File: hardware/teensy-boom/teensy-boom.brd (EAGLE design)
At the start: 160 x 100 mm, 5 parts

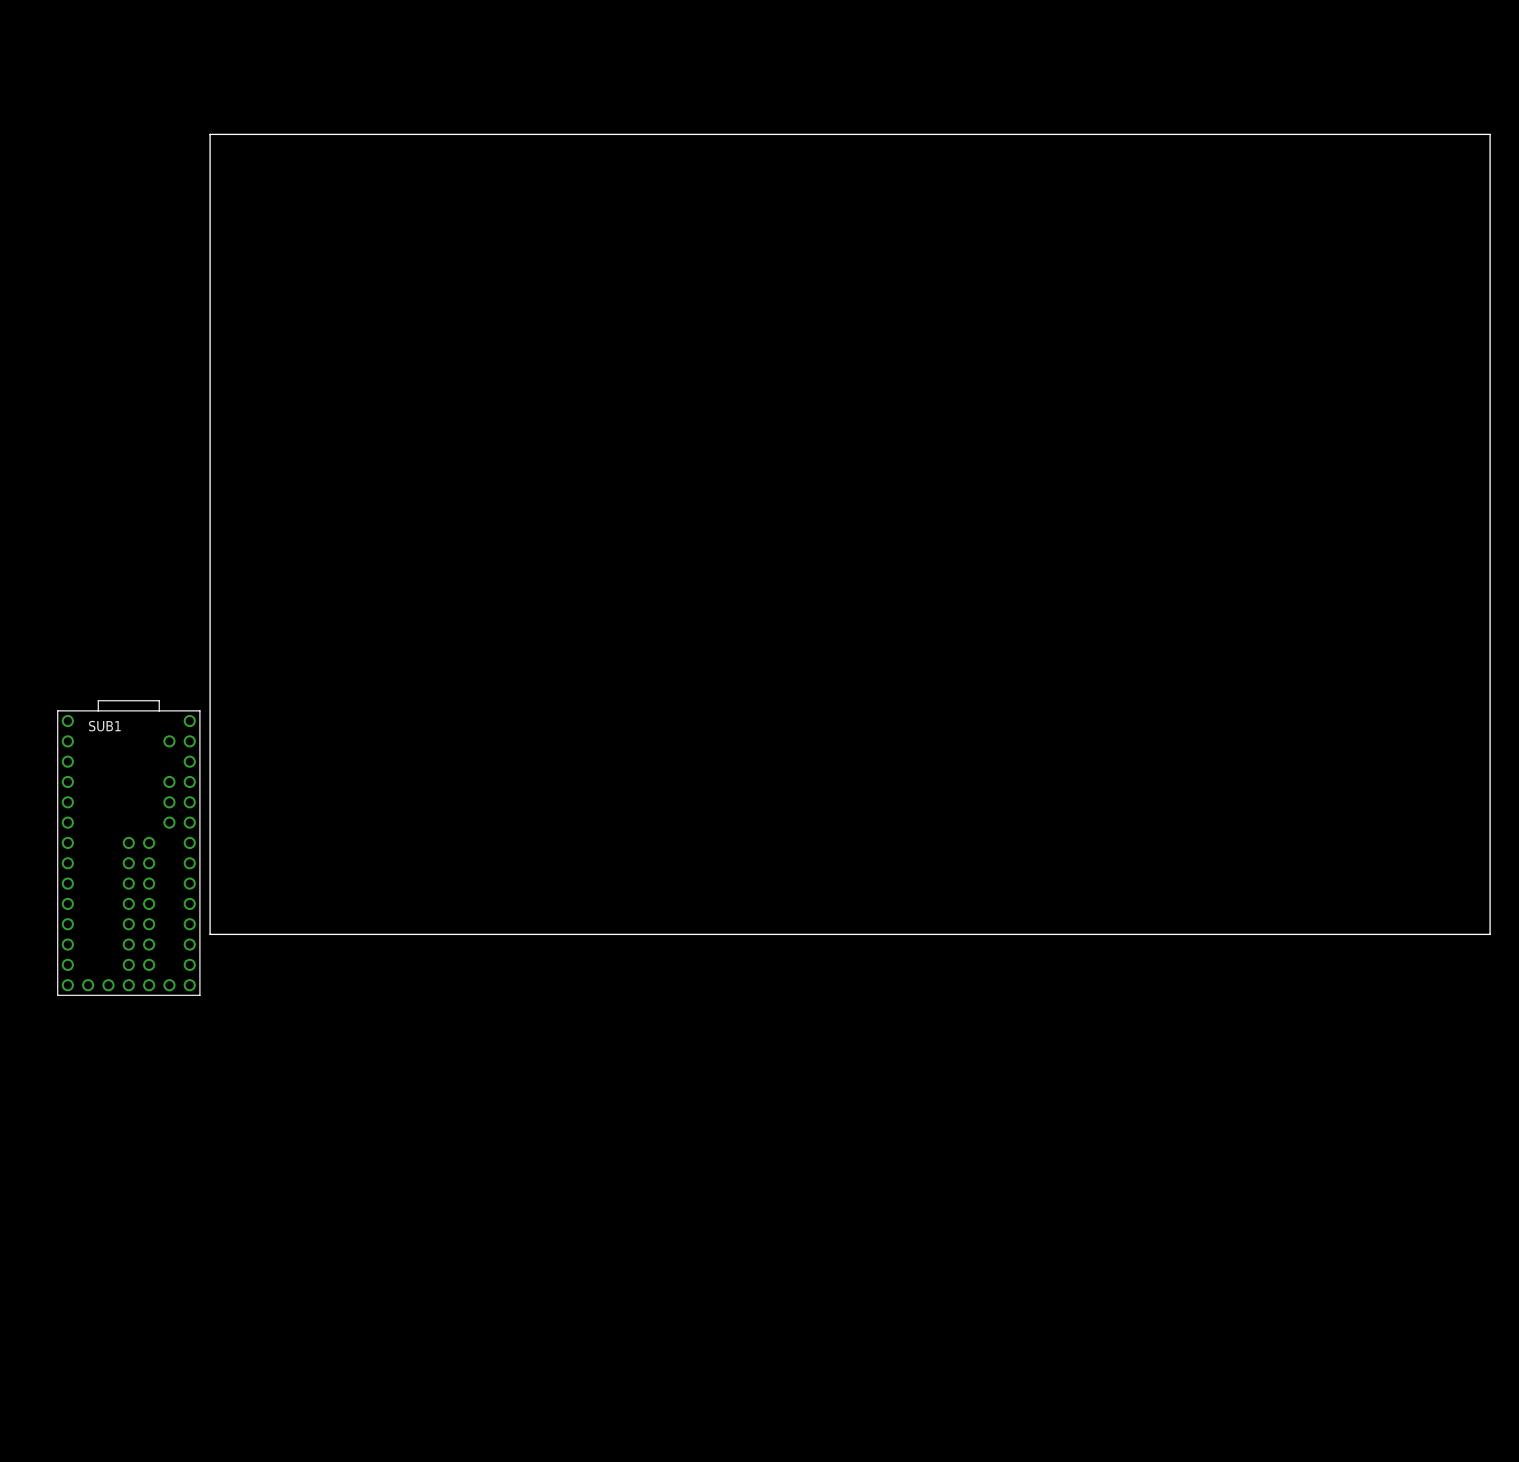
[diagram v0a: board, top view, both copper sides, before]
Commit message: More PCB work
Added knobs, buttons, connectors, MIDI.

Basic PCB alignment in place...~6"x4"
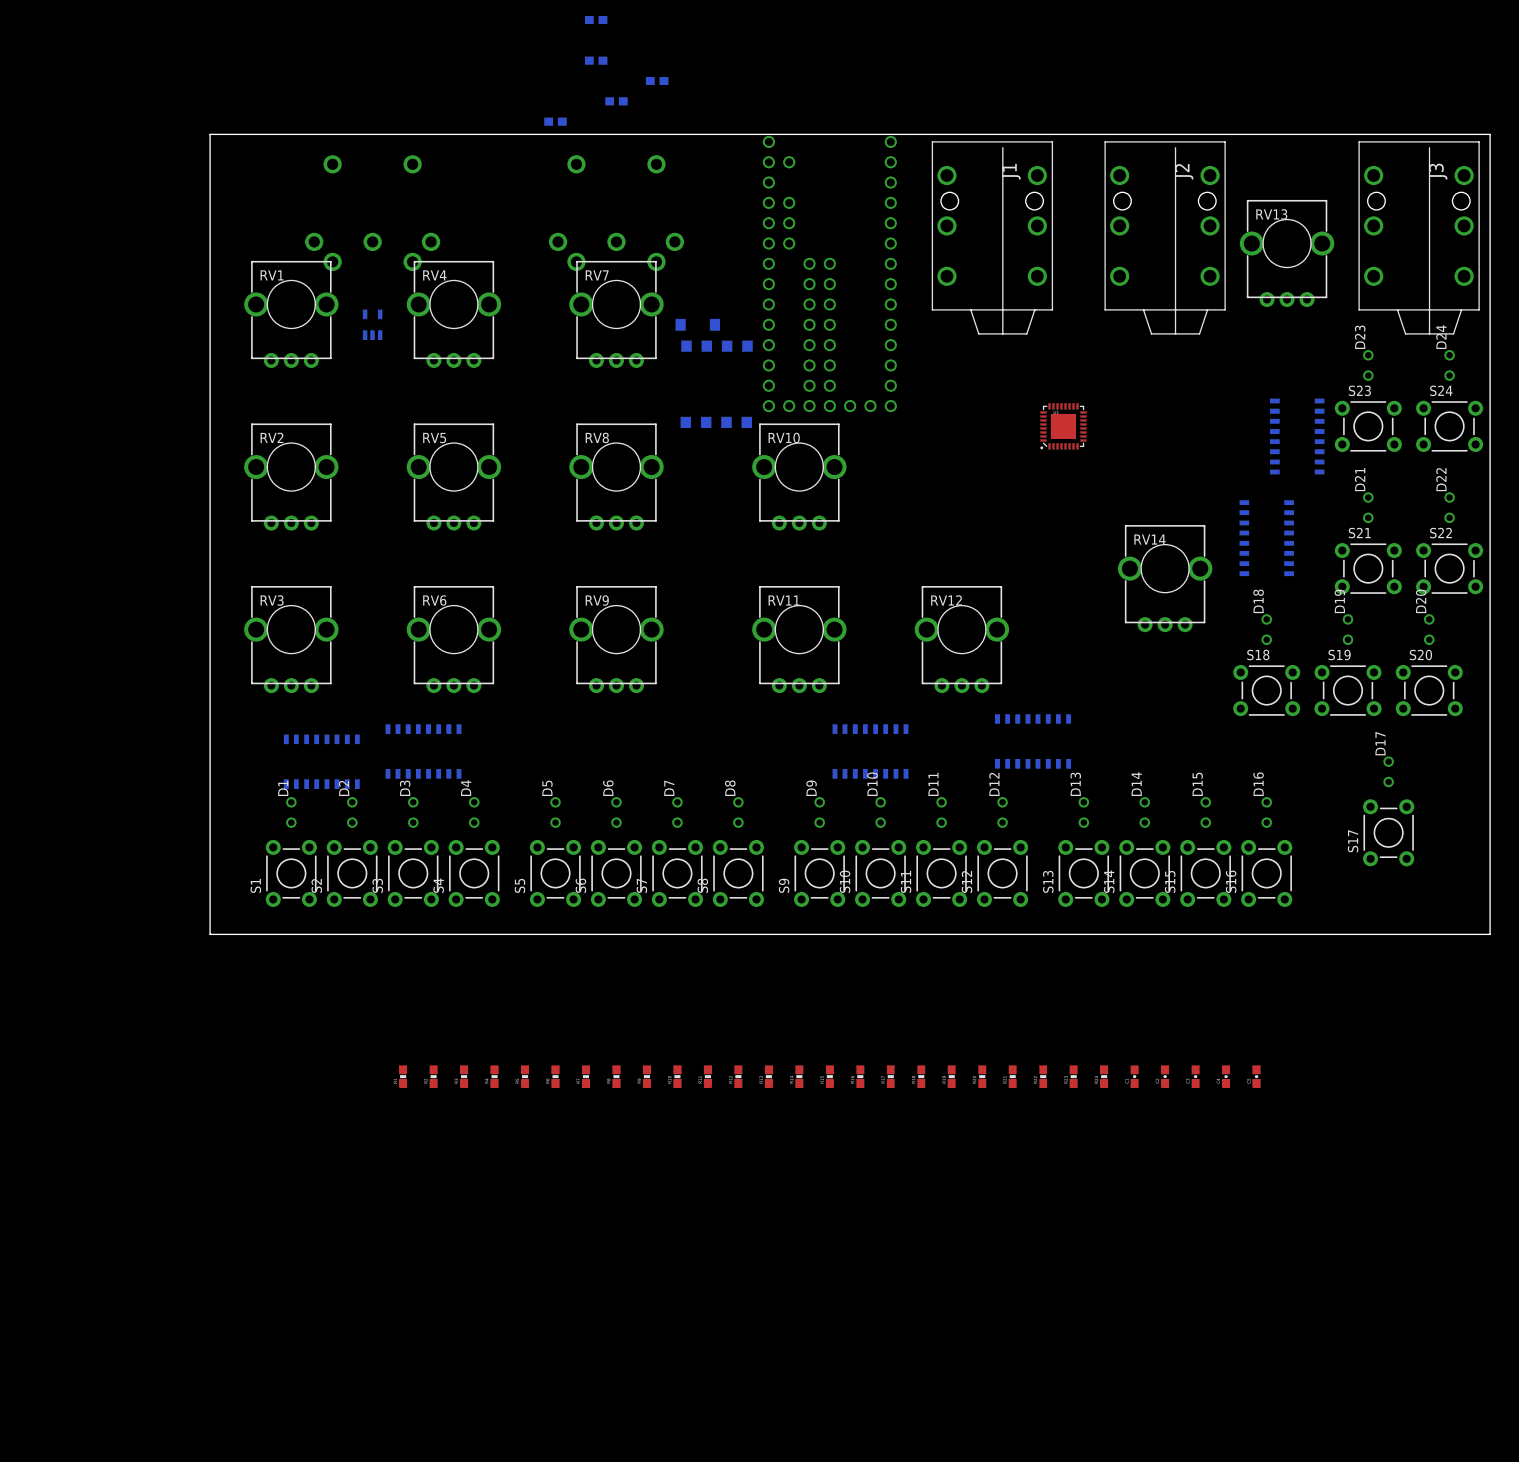
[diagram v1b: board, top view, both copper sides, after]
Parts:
- added C1, C2, C3, C4, C5, C6: 0.1uF, SparkFun-Capacitors:0603-CAP
- added D1, D10, D11, D12, D13, D14, D15, D16, D17, D18, D19, D2, D20, D21, D22, D23, D24, D3, D4, D5, D6, D7, D8, D9: (no value), SparkFun-LED:LED3MM-NS
- added D25: MBRA140, SparkFun-DiscreteSemi:SMA-DIODE
- added J1, J2, J3: AUDIO-JACK4-.25-HORIZ-TRS, SparkFun-Connectors:AUDIO-JACK-.25-INCH-HORIZ-PTH
- added J4, J5: 5-PIN-CIRCULAR-DINNEW, Testing:5-PIN-DIN-RA-PCB-NEW
- added R1, R10, R11, R12, R13, R14, R15, R16, R17, R18, R19, R2, R20, R21, R22, R23, R24, R3, R4, R5, R6, R7, R8, R9: 330, SparkFun-Resistors:0603-RES
- added R25, R26, R27, R28: 220, SparkFun-Resistors:0603-RES
- added RV1, RV10, RV11, RV12, RV13, RV14, RV2, RV3, RV4, RV5, RV6, RV7, RV8, RV9: (no value), SparkFun-Electromechanical:ALPS_POT_KIT
- added S1, S10, S11, S12, S13, S14, S15, S16, S17, S18, S19, S2, S20, S21, S22, S23, S24, S3, S4, S5, S6, S7, S8, S9: 6mm-TACT, SparkFun-Electromechanical:TACTILE-PTH
- added U1: SGTL5000, teensy-synth:QFN-32
- added U2, U3, U4: 74hc165, teensy-synth:SO16
- added U5, U6, U7: 74hc595, teensy-synth:SO16
- added U8: 6N138M, SparkFun-DiscreteSemi:8-SMD
- added U9: 74AHC1G125, SparkFun-DigitalIC:SOT23-5
- moved SUB1 127.9 mm to (86.4, 64.8), flipped to the bottom
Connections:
- new net 5V: R26.2, R28.2, U8.8, U9.5
- new net GND: J5.2, U8.5, U9.1, U9.3
- new net N$1: U9.2
- new net N$2: J4.4, R25.1
- new net N$3: D25.C, R25.2, U8.2
- new net N$4: D25.A, J4.5, U8.3
- new net N$5: R26.1, U8.6
- new net N$7: R27.1, U9.4
- new net N$8: J5.5, R27.2
- new net N$9: J5.4, R28.1

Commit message: More work on PCB/Schem
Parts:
- D1, D10, D11, D12, D13, D14, D15, D16, D17, D18, D19, D2, D20, D21, D22, D23, D24, D3, D4, D5, D6, D7, D8, D9: value (none) -> red
- RV1, RV10, RV11, RV12, RV13, RV14, RV2, RV3, RV4, RV5, RV6, RV7, RV8, RV9: value (none) -> 100k
- moved R16 118.4 mm to (154.9, 74.9), flipped to the bottom, turned to 180 degrees
- moved R15 114.6 mm to (144.8, 74.9), flipped to the bottom, turned to 180 degrees
- moved R14 110.5 mm to (154.9, 57.1), flipped to the bottom, turned to 180 degrees
- moved R13 106.0 mm to (144.8, 57.1), flipped to the bottom, turned to 180 degrees
- moved R12 104.3 mm to (152.4, 40.6), flipped to the bottom, turned to 180 degrees
- moved R9 101.2 mm to (147.3, 22.9), flipped to the bottom, turned to 180 degrees
- moved R11 99.1 mm to (142.2, 40.6), flipped to the bottom, turned to 180 degrees
- moved C6 98.4 mm to (135.9, 68.6)
- moved C1 97.1 mm to (27.9, 24.1), flipped to the bottom
- moved R10 94.0 mm to (132.1, 40.6), flipped to the bottom, turned to 180 degrees
- moved C2 71.9 mm to (61.0, 24.1), flipped to the bottom
- moved C5 61.0 mm to (132.1, 43.2), flipped to the bottom, turned to 180 degrees
- moved C3 53.2 mm to (88.9, 22.9), flipped to the bottom
- moved C4 45.5 mm to (109.2, 24.1), flipped to the bottom
- moved U8 40.4 mm to (35.6, 97.8)
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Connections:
- new net AGND: RV1.P$3, RV10.P$3, RV11.P$3, RV12.P$3, RV13.P$3, RV14.P$3, RV2.P$3, RV3.P$3, RV4.P$3, RV5.P$3, RV6.P$3, RV7.P$3, RV8.P$3, RV9.P$3, SUB1.RAGND, U1.7
- new net AREF: RV1.P$1, RV10.P$1, RV11.P$1, RV12.P$1, RV13.P$1, RV14.P$1, RV2.P$1, RV3.P$1, RV4.P$1, RV5.P$1, RV6.P$1, RV7.P$1, RV8.P$1, RV9.P$1, SUB1.BAREF
- new net BCLK: SUB1.L9, U1.24
- new net CYM-DECAY: RV11.P$2, SUB1.B27
- new net CYM-MIX: RV10.P$2, SUB1.EA14
- new net HAT-DECAY: RV12.P$2, SUB1.B28
- new net I2CRX: SUB1.R13, U1.25
- new net I2CTX: SUB1.R22, U1.26
- new net KIK-DECAY: RV3.P$2, SUB1.R17
- new net KIK-MOD: RV2.P$2, SUB1.R16
- new net KIK-PITCH: RV1.P$2, SUB1.R15
- new net LRCLK: SUB1.R23, U1.23
- new net MCLK: SUB1.L11, U1.21
- new net N$10: D2.K, R2.2
- new net N$11: D3.K, R3.2
- new net N$12: D4.K, R4.2
- new net N$13: D5.K, R5.2
- new net N$14: D6.K, R6.2
- new net N$15: D7.K, R7.2
- new net N$16: D8.K, R8.2
- new net N$17: D9.K, R17.2
- new net N$18: D10.K, R18.2
- new net N$19: D11.K, R19.2
- new net N$20: D12.K, R20.2
- new net N$21: D13.K, R21.2
- new net N$22: D14.K, R22.2
- new net N$23: D15.K, R23.2
- new net N$24: D16.K, R24.2
- new net N$26: D17.K, R9.2
- new net N$27: D18.K, R10.2
- new net N$28: D19.K, R11.2
- new net N$29: D20.K, R12.2
- new net N$30: D21.K, R13.2
- new net N$31: D22.K, R14.2
- new net N$32: D23.K, R15.2
- new net N$33: D24.K, R16.2
- new net N$34: D5.A, U5.3
- new net N$35: D4.A, U5.4
- new net N$36: D3.A, U5.5
- new net N$37: D2.A, U5.6
- new net N$38: D1.A, U5.7
- new net N$39: D6.A, U5.2
- new net N$40: D7.A, U5.1
- new net N$41: D8.A, U5.15
- new net N$42: D12.A, U6.4
- new net N$43: D11.A, U6.5
- new net N$44: D10.A, U6.6
- new net N$45: D9.A, U6.7
- new net N$46: D13.A, U6.3
- new net N$47: D14.A, U6.2
- new net N$48: D15.A, U6.1
- new net N$49: D16.A, U6.15
- new net N$50: D20.A, U7.4
- new net N$51: D19.A, U7.5
- new net N$52: D18.A, U7.6
- new net N$53: D17.A, U7.7
- new net N$54: D21.A, U7.3
- new net N$55: D24.A, U7.15
- new net N$56: D23.A, U7.1
- new net N$57: D22.A, U7.2
- new net N$6: D1.K, R1.2
- new net SCL: SUB1.R19, U1.29
- new net SDA: SUB1.R18, U1.27
- new net SNR-DECAY: RV6.P$2, SUB1.BA10
- new net SNR-MIX: RV5.P$2, SUB1.R21
- new net SNR-PITCH: RV4.P$2, SUB1.R20
- new net TEMPO: RV14.P$2, SUB1.B29
- new net TOM-2ND: RV8.P$2, SUB1.BA12
- new net TOM-DECAY: RV9.P$2, SUB1.BA13
- new net TOM-PITCH: RV7.P$2, SUB1.BA11
- new net VOLUME: RV13.P$2, SUB1.B30
- net GND: now also R1.1, R10.1, R11.1, R12.1, R13.1, R14.1, R15.1, R16.1, R17.1, R18.1, R19.1, R2.1, R20.1, R21.1, R22.1, R23.1, R24.1, R3.1, R4.1, R5.1, R6.1, R7.1, R8.1, R9.1, SUB1.BGND, SUB1.EGND, SUB1.LGND, U1.1, U1.3, U1.31, U1.32, U1.EP
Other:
- board size 160 x 100 mm -> 160 x 108 mm

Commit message: More work on BOOM schem/PCB.
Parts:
- removed C4, C5, C6: 0.1uF, SparkFun-Capacitors:0603-CAP
- added C10, C7, C8, C9: 2.2uF, SparkFun-Capacitors:0805-CAP
- added C11: 0.1u, SparkFun-Capacitors:0805
- added C12, C13, C14: 0.1uF, SparkFun-Capacitors:0603-CAP
- added FRAME5: FRAME-LETTERNO_PACKAGE, SparkFun-Aesthetics:DUMMY
- added J6: Inputs, SparkFun-Connectors:1X03_LOCK
- added R29, R30, R31, R32, R33, R34, R35, R36, R37, R38, R39, R40, R41, R42, R43, R44, R45, R46, R47, R48, R49, R50, R51, R52: 100k, SparkFun-Resistors:0805
- J1: value AUDIO-JACK4-.25-HORIZ-TRS -> LEFT-OUT
- J2: value AUDIO-JACK4-.25-HORIZ-TRS -> RIGHT-OUT
- J3: value AUDIO-JACK4-.25-HORIZ-TRS -> PHONES
- moved C2 17.8 mm to (43.2, 24.1), turned to 270 degrees
- moved U2 17.8 mm to (36.8, 24.1)
- moved C3 12.7 mm to (76.2, 22.9)
- moved U7 2.84 mm to (133.3, 63.5)
- turned C1 to 270 degrees
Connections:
- new net 3.3V: C1.1, C12.1, C13.1, C14.1, C2.1, C3.1, R29.2, R30.2, R31.2, R32.2, R33.2, R34.2, R35.2, R36.2, R37.2, R38.2, R39.2, R40.2, R41.2, R42.2, R43.2, R44.2, R45.2, R46.2, R47.2, R48.2, R49.2, R50.2, R51.2, R52.2, U2.16, U3.16, U4.16, U5.16, U6.16, U7.16
- new net N$25: C8.1, J2.TIP
- new net N$58: C7.2, J1.TIP
- new net N$59: C8.2, U1.11
- new net N$60: C7.1, U1.12
- new net N$61: C10.2, U1.13
- new net N$62: C9.2, U1.14
- new net N$63: J3.TIP, U1.6
- new net N$64: J3.RING, U1.2
- new net N$65: J3.SLEEVE, U1.4
- new net N$66: C9.1, J6.2
- new net N$67: C10.1, J6.3
- new net N$68: C11.1, U1.10
- new net N$69: R35.1, S7.1, U2.5
- new net N$70: R29.1, S1.1, U2.11
- new net N$71: R30.1, S2.1, U2.12
- new net N$72: R31.1, S3.1, U2.13
- new net N$73: R32.1, S4.1, U2.14
- new net N$74: R33.1, S5.1, U2.3
- new net N$75: R34.1, S6.1, U2.4
- new net N$76: R36.1, S8.1, U2.6
- new net N$77: R37.1, S9.1, U3.11
- new net N$78: R38.1, S10.1, U3.12
- new net N$79: R39.1, S11.1, U3.13
- new net N$80: R40.1, S12.1, U3.14
- new net N$81: R41.1, S13.1, U3.3
- new net N$82: R42.1, S14.1, U3.4
- new net N$83: R43.1, S15.1, U3.5
- new net N$84: R44.1, S16.1, U3.6
- new net N$840: R52.1, S24.1, U4.6
- new net N$85: R45.1, S17.1, U4.11
- new net N$86: R46.1, S18.1, U4.12
- new net N$87: R47.1, S19.1, U4.13
- new net N$88: R48.1, S20.1, U4.14
- new net N$89: R49.1, S21.1, U4.3
- new net N$90: R50.1, S22.1, U4.4
- new net N$91: R51.1, S23.1, U4.5
- net AGND: now also J1.SLEEVE, J2.SLEEVE, J6.1
- net GND: now also C1.2, C11.2, C12.2, C13.2, C14.2, C2.2, C3.2, S1.3, S10.3, S11.3, S12.3, S13.3, S14.3, S15.3, S16.3, S17.3, S18.3, S19.3, S2.3, S20.3, S21.3, S22.3, S23.3, S24.3, S3.3, S4.3, S5.3, S6.3, S7.3, S8.3, S9.3, U2.8, U3.8, U4.8, U5.8, U6.8, U7.8
